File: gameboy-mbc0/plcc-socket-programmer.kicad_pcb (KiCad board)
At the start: 2 copper layers, 2 parts, among them P1 CONN_01X32, U1 SST39SF010

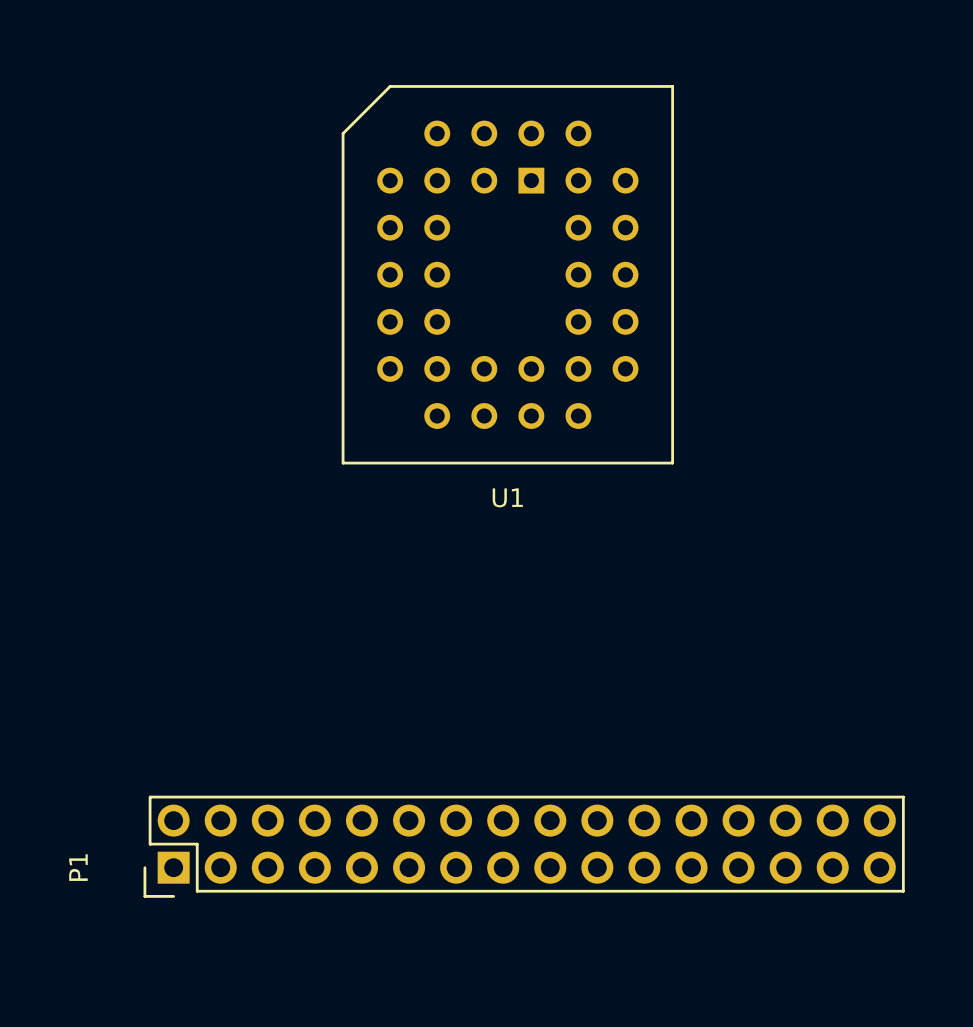
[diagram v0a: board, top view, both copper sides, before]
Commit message: wired up data lines
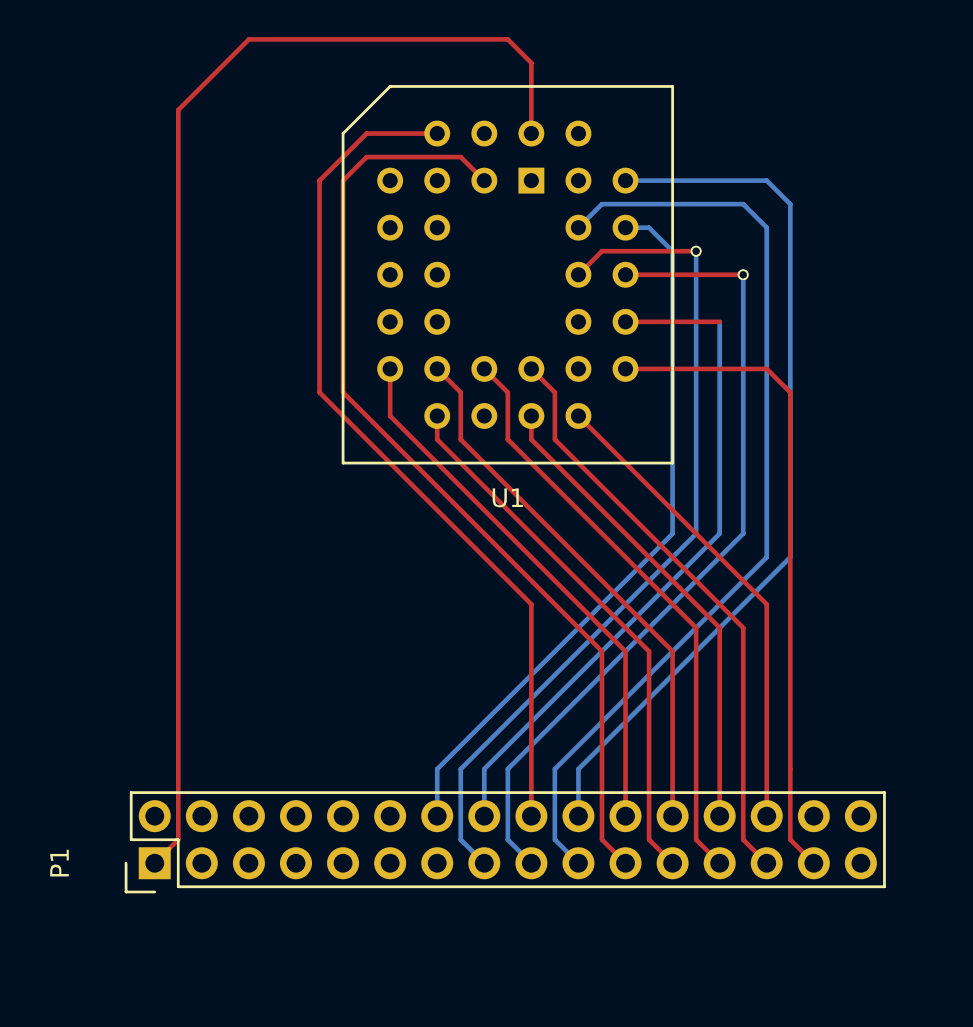
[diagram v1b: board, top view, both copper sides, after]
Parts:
- moved P1 1.05 mm to (125.7, 143.5)
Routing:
- net VCC: track 0.00 -> 66.1 mm
- net Net-(P1-Pad21): track 0.00 -> 51.8 mm
- net Net-(P1-Pad19): track 0.00 -> 50.8 mm
- net Net-(P1-Pad20): track 0.00 -> 47.2 mm
- net Net-(P1-Pad18): track 0.00 -> 46.4 mm
- net Net-(P1-Pad15): track 0.00 -> 45.7 mm, vias 0 -> 1
- net Net-(P1-Pad17): track 0.00 -> 43.9 mm, vias 0 -> 1
- net Net-(P1-Pad14): track 0.00 -> 38.8 mm
- net Net-(P1-Pad16): track 0.00 -> 37.0 mm
- net Net-(P1-Pad29): track 0.00 -> 35.3 mm
- net Net-(P1-Pad25): track 0.00 -> 31.9 mm
- net Net-(P1-Pad27): track 0.00 -> 31.9 mm
- net Net-(P1-Pad23): track 0.00 -> 29.4 mm
- net Net-(P1-Pad24): track 0.00 -> 29.4 mm
- net Net-(P1-Pad22): track 0.00 -> 29.4 mm
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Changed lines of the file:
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@@
   (general
     (links 30)
-    (no_connects 30)
-    (area 0 0 0 0)
+    (no_connects 14)
+    (area 120.675 101.324999 166.825001 148.783333)
     (thickness 1.6)
     (drawings 0)
-    (tracks 0)
+    (tracks 83)
     (zones 0)
     (modules 2)
@@
   )
   (module Pin_Headers:Pin_Header_Straight_2x16 (layer F.Cu)
-    (at 126.75 143.75 90)
+    (at 125.73 143.51 90)
     (descr "Through hole pin header")
     (tags "pin header")
@@
       (net 34 "Net-(U1-Pad30)"))
   )
+  (segment (start 125.73 143.51) (end 127 142.24) (width 0.25) (layer F.Cu) (net 1))
+  (segment (start 146.05 100.33) (end 146.05 104.14) (width 0.25) (layer F.Cu) (net 1))
+  (segment (start 144.78 99.06) (end 146.05 100.33) (width 0.25) (layer F.Cu) (net 1))
+  (segment (start 130.81 99.06) (end 144.78 99.06) (width 0.25) (layer F.Cu) (net 1))
+  (segment (start 127 102.87) (end 130.81 99.06) (width 0.25) (layer F.Cu) (net 1))
+  (segment (start 127 142.24) (end 127 102.87) (width 0.25) (layer F.Cu) (net 1))
+  (segment (start 153.67 110.49) (end 152.4 109.22) (width 0.25) (layer B.Cu) (net 14))
+  (segment (start 153.67 125.73) (end 153.67 110.49) (width 0.25) (layer B.Cu) (net 14))
+  (segment (start 140.97 138.43) (end 153.67 125.73) (width 0.25) (layer B.Cu) (net 14))
+  (segment (start 140.97 140.97) (end 140.97 138.43) (width 0.25) (layer B.Cu) (net 14))
+  (segment (start 152.4 109.22) (end 151.13 109.22) (width 0.25) (layer B.Cu) (net 14) (status 800000))
+  (segment (start 142.24 138.43) (end 142.24 142.24) (width 0.25) (layer B.Cu) (net 15))
+  (segment (start 142.24 138.43) (end 154.94 125.73) (width 0.25) (layer B.Cu) (net 15))
+  (segment (start 154.94 125.73) (end 154.94 110.49) (width 0.25) (layer B.Cu) (net 15))
+  (via (at 154.94 110.49) (size 0.6) (drill 0.4) (layers F.Cu B.Cu) (net 15))
+  (segment (start 154.94 110.49) (end 149.86 110.49) (width 0.25) (layer F.Cu) (net 15))
+  (segment (start 148.59 111.76) (end 149.86 110.49) (width 0.25) (layer F.Cu) (net 15))
+  (segment (start 142.24 142.24) (end 143.51 143.51) (width 0.25) (layer B.Cu) (net 15))
+  (segment (start 156.21 114.3) (end 151.13 114.3) (width 0.25) (layer F.Cu) (net 16))
+  (segment (start 143.51 140.97) (end 143.51 138.43) (width 0.25) (layer B.Cu) (net 16))
+  (segment (start 143.51 138.43) (end 156.21 125.73) (width 0.25) (layer B.Cu) (net 16))
+  (segment (start 156.21 125.73) (end 156.21 114.3) (width 0.25) (layer B.Cu) (net 16))
+  (segment (start 144.78 138.43) (end 144.78 142.24) (width 0.25) (layer B.Cu) (net 17))
+  (segment (start 144.78 138.43) (end 157.48 125.73) (width 0.25) (layer B.Cu) (net 17))
+  (segment (start 157.48 125.73) (end 157.48 111.76) (width 0.25) (layer B.Cu) (net 17))
+  (via (at 157.48 111.76) (size 0.6) (drill 0.4) (layers F.Cu B.Cu) (net 17))
+  (segment (start 151.13 111.76) (end 157.48 111.76) (width 0.25) (layer F.Cu) (net 17))
+  (segment (start 144.78 142.24) (end 146.05 143.51) (width 0.25) (layer B.Cu) (net 17))
+  (segment (start 146.05 140.97) (end 146.05 129.54) (width 0.25) (layer F.Cu) (net 18))
+  (segment (start 137.16 104.14) (end 140.97 104.14) (width 0.25) (layer F.Cu) (net 18))
+  (segment (start 134.62 106.68) (end 137.16 104.14) (width 0.25) (layer F.Cu) (net 18))
+  (segment (start 134.62 118.11) (end 134.62 106.68) (width 0.25) (layer F.Cu) (net 18))
+  (segment (start 146.05 129.54) (end 134.62 118.11) (width 0.25) (layer F.Cu) (net 18))
+  (segment (start 158.75 109.22) (end 157.48 107.95) (width 0.25) (layer B.Cu) (net 19))
+  (segment (start 148.59 143.51) (end 147.32 142.24) (width 0.25) (layer B.Cu) (net 19))
+  (segment (start 158.75 127) (end 158.75 109.22) (width 0.25) (layer B.Cu) (net 19))
+  (segment (start 147.32 138.43) (end 158.75 127) (width 0.25) (layer B.Cu) (net 19))
+  (segment (start 147.32 138.43) (end 147.32 142.24) (width 0.25) (layer B.Cu) (net 19))
+  (segment (start 149.86 107.95) (end 148.59 109.22) (width 0.25) (layer B.Cu) (net 19) (status 800000))
+  (segment (start 157.48 107.95) (end 149.86 107.95) (width 0.25) (layer B.Cu) (net 19))
+  (segment (start 160.02 107.95) (end 158.75 106.68) (width 0.25) (layer B.Cu) (net 20))
+  (segment (start 160.02 127) (end 160.02 107.95) (width 0.25) (layer B.Cu) (net 20))
+  (segment (start 148.59 138.43) (end 160.02 127) (width 0.25) (layer B.Cu) (net 20))
+  (segment (start 148.59 140.97) (end 148.59 138.43) (width 0.25) (layer B.Cu) (net 20))
+  (segment (start 158.75 106.68) (end 151.13 106.68) (width 0.25) (layer B.Cu) (net 20) (status 800000))
+  (segment (start 151.13 143.51) (end 149.86 142.24) (width 0.25) (layer F.Cu) (net 21))
+  (segment (start 142.24 105.41) (end 143.51 106.68) (width 0.25) (layer F.Cu) (net 21))
+  (segment (start 137.16 105.41) (end 142.24 105.41) (width 0.25) (layer F.Cu) (net 21))
+  (segment (start 135.89 106.68) (end 137.16 105.41) (width 0.25) (layer F.Cu) (net 21))
+  (segment (start 135.89 118.11) (end 135.89 106.68) (width 0.25) (layer F.Cu) (net 21))
+  (segment (start 149.86 132.08) (end 135.89 118.11) (width 0.25) (layer F.Cu) (net 21))
+  (segment (start 149.86 142.24) (end 149.86 132.08) (width 0.25) (layer F.Cu) (net 21))
+  (segment (start 151.13 140.97) (end 151.13 132.08) (width 0.25) (layer F.Cu) (net 22))
+  (segment (start 138.43 119.38) (end 138.43 116.84) (width 0.25) (layer F.Cu) (net 22))
+  (segment (start 151.13 132.08) (end 138.43 119.38) (width 0.25) (layer F.Cu) (net 22))
+  (segment (start 153.67 143.51) (end 152.4 142.24) (width 0.25) (layer F.Cu) (net 23))
+  (segment (start 140.97 120.65) (end 140.97 119.38) (width 0.25) (layer F.Cu) (net 23))
+  (segment (start 152.4 132.08) (end 140.97 120.65) (width 0.25) (layer F.Cu) (net 23))
+  (segment (start 152.4 142.24) (end 152.4 132.08) (width 0.25) (layer F.Cu) (net 23))
+  (segment (start 153.67 140.97) (end 153.67 132.08) (width 0.25) (layer F.Cu) (net 24))
+  (segment (start 142.24 118.11) (end 140.97 116.84) (width 0.25) (layer F.Cu) (net 24))
+  (segment (start 142.24 120.65) (end 142.24 118.11) (width 0.25) (layer F.Cu) (net 24))
+  (segment (start 153.67 132.08) (end 142.24 120.65) (width 0.25) (layer F.Cu) (net 24))
+  (segment (start 156.21 143.51) (end 154.94 142.24) (width 0.25) (layer F.Cu) (net 25))
+  (segment (start 144.78 118.11) (end 143.51 116.84) (width 0.25) (layer F.Cu) (net 25))
+  (segment (start 144.78 120.65) (end 144.78 118.11) (width 0.25) (layer F.Cu) (net 25))
+  (segment (start 154.94 130.81) (end 144.78 120.65) (width 0.25) (layer F.Cu) (net 25))
+  (segment (start 154.94 142.24) (end 154.94 130.81) (width 0.25) (layer F.Cu) (net 25))
+  (segment (start 156.21 140.97) (end 156.21 130.81) (width 0.25) (layer F.Cu) (net 26))
+  (segment (start 146.05 120.65) (end 146.05 119.38) (width 0.25) (layer F.Cu) (net 26))
+  (segment (start 156.21 130.81) (end 146.05 120.65) (width 0.25) (layer F.Cu) (net 26))
+  (segment (start 158.75 143.51) (end 157.48 142.24) (width 0.25) (layer F.Cu) (net 27))
+  (segment (start 147.32 118.11) (end 146.05 116.84) (width 0.25) (layer F.Cu) (net 27))
+  (segment (start 147.32 120.65) (end 147.32 118.11) (width 0.25) (layer F.Cu) (net 27))
+  (segment (start 157.48 130.81) (end 147.32 120.65) (width 0.25) (layer F.Cu) (net 27))
+  (segment (start 157.48 142.24) (end 157.48 130.81) (width 0.25) (layer F.Cu) (net 27))
+  (segment (start 158.75 140.97) (end 158.75 129.54) (width 0.25) (layer F.Cu) (net 28))
+  (segment (start 158.75 129.54) (end 148.59 119.38) (width 0.25) (layer F.Cu) (net 28))
+  (segment (start 161.29 143.51) (end 160.02 142.24) (width 0.25) (layer F.Cu) (net 29))
+  (segment (start 158.75 116.84) (end 151.13 116.84) (width 0.25) (layer F.Cu) (net 29))
+  (segment (start 160.02 118.11) (end 158.75 116.84) (width 0.25) (layer F.Cu) (net 29))
+  (segment (start 160.02 138.43) (end 160.02 118.11) (width 0.25) (layer F.Cu) (net 29))
+  (segment (start 160.02 142.24) (end 160.02 138.43) (width 0.25) (layer F.Cu) (net 29))
 )

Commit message: wired up programmer
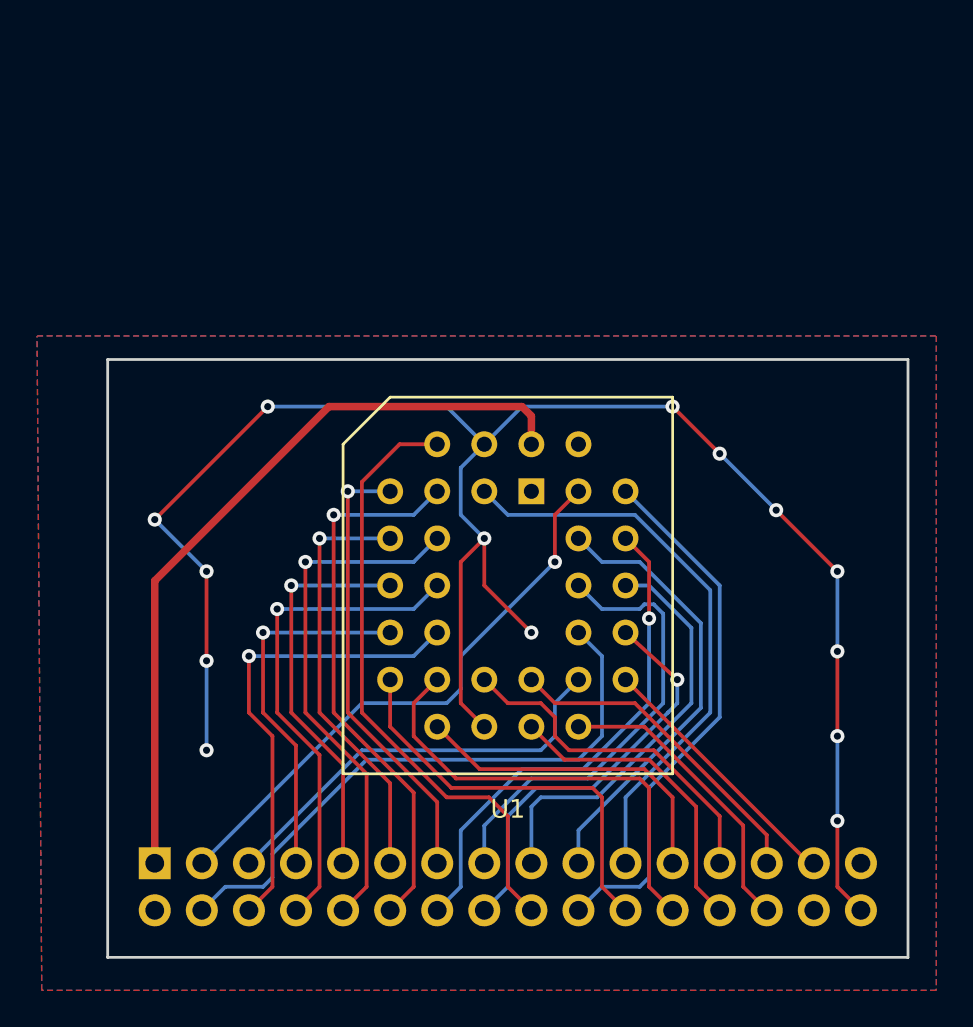
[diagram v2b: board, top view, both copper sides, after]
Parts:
- P1: moved to B.Cu
- moved U1 16.8 mm to (144.8, 128.5)
- turned P1 to 270 degrees
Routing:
- net GND: track 0.00 -> 100.6 mm, vias 0 -> 14
- net Net-(P1-Pad4): track 0.00 -> 32.3 mm
- net Net-(P1-Pad3): track 0.00 -> 31.2 mm, vias 0 -> 1
- net Net-(P1-Pad12): track 0.00 -> 29.8 mm, vias 0 -> 1
- net Net-(P1-Pad10): track 0.00 -> 28.3 mm, vias 0 -> 1
- net Net-(P1-Pad8): track 0.00 -> 26.9 mm, vias 0 -> 1
- net Net-(P1-Pad19): track 50.8 -> 24.2 mm
- net Net-(P1-Pad6): track 0.00 -> 25.5 mm, vias 0 -> 1
- net VCC: track 66.1 -> 41.2 mm
- net Net-(P1-Pad13): track 0.00 -> 24.4 mm, vias 0 -> 1
- net Net-(P1-Pad5): track 0.00 -> 22.9 mm
- net Net-(P1-Pad11): track 0.00 -> 22.9 mm, vias 0 -> 1
- net Net-(P1-Pad9): track 0.00 -> 21.5 mm, vias 0 -> 1
- net Net-(P1-Pad17): track 43.9 -> 22.6 mm, vias 1 -> 0
- net Net-(P1-Pad29): track 35.3 -> 14.3 mm
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- added copper zone on B.Cu, net GND
- added copper zone on F.Cu, net GND
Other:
- board outline added: 43.2 x 32.3 mm
- net class Default: clearance 0.2 -> 0.2032; trace_width 0.25 -> 0.2032; via_dia 0.6 -> 0.762; via_drill 0.4 -> 0.381
- rule trace_clearance: 0.2 -> 0.2032
- rule trace_min: 0.2 -> 0.1524
- rule via_min_drill: 0.3 -> 0.3302
- rule via_min_size: 0.4 -> 0.6858

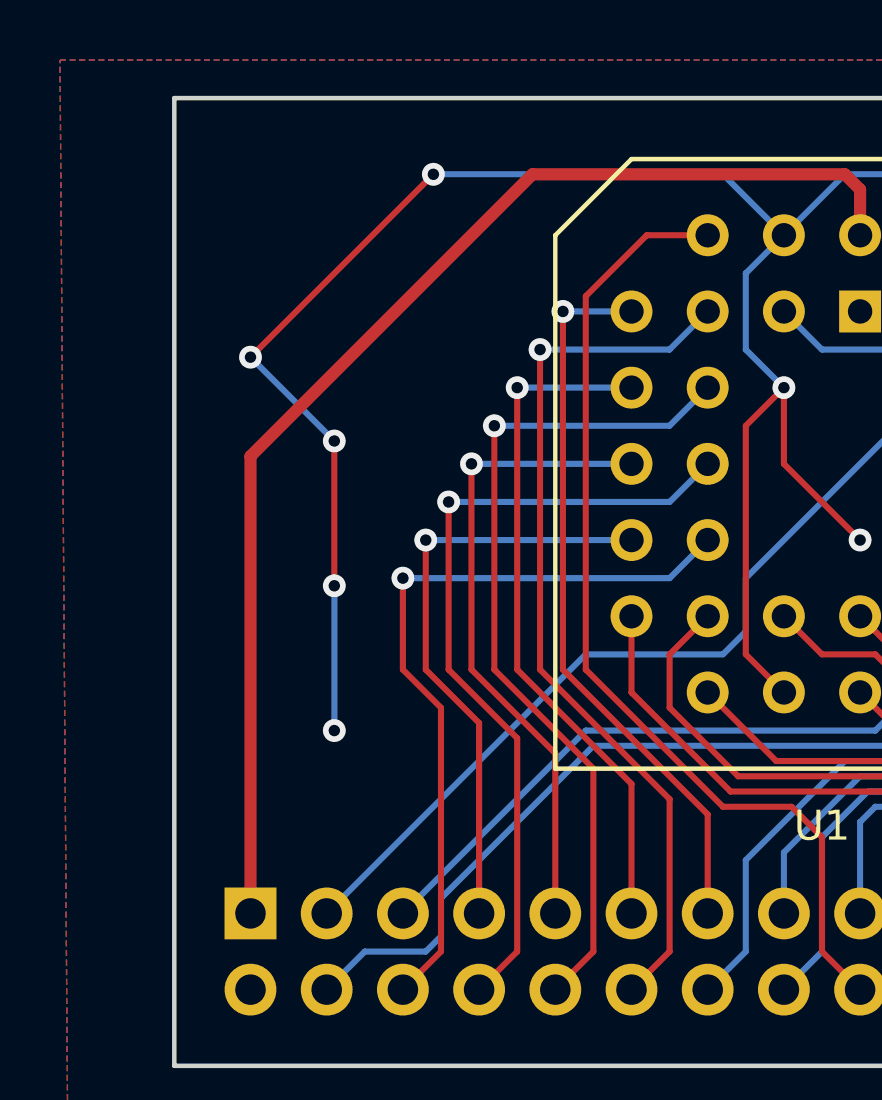
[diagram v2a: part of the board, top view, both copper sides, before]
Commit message: added power smoothing capacitors and board outline
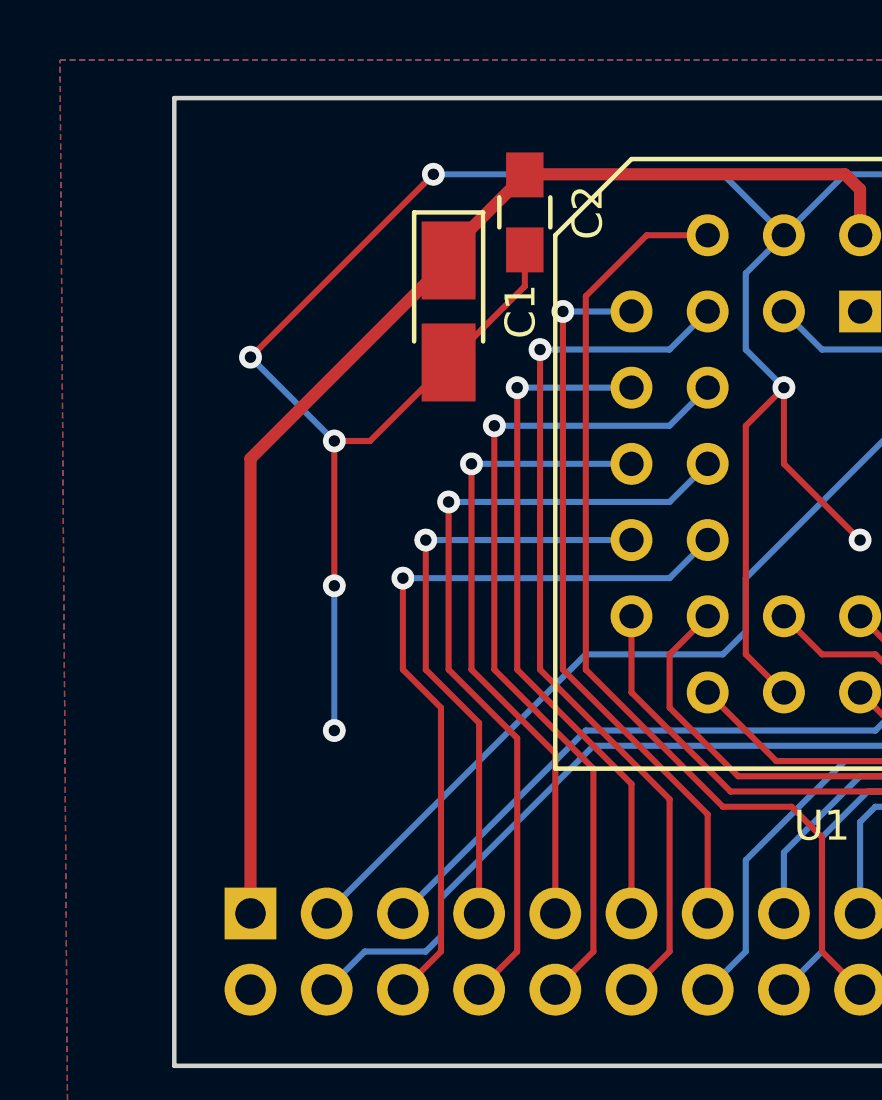
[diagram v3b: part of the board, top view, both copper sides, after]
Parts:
- added C1: 10uF, Capacitors_Tantalum_SMD:Tantalum_Case-R_EIA-2012-12_Hand, F.Cu at (132.3, 123.4)
- added C2: 0.1uF, Capacitors_SMD:C_0805_HandSoldering, F.Cu at (134.9, 120.1)
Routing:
- net GND: track 100.6 -> 110.3 mm
